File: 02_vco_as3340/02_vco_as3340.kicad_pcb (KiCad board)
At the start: 2 copper layers, 60 x 108 mm, 98 parts, among them J10 SINE OUT, J3 SYNC IN, J4 FM IN, J5 PWM CV IN, J6 1V per O IN, J7 SQUARE OUT, J8 SAW OUT, J9 TRI OUT, Q1 BC847, Q2 BC847, SW2 SW_SPDT, U1 TL072, U2 AS3340, U3 TL074

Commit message: added diodes
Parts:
- added D3: 1N5819WS, Diode_SMD:D_SOD-323, B.Cu at (21.0, 88.3)
- added D4: 1N5819WS, Diode_SMD:D_SOD-323, B.Cu at (37.5, 87.6)
- C7, C8: value 47uF -> 20uF
- SW1: footprint cynthia:switch_linear_1x4 -> cynthia:switch_linear_2x4
- SW2: footprint cynthia:switch -> cynthia:switch_spdt
- moved C7 1.13 mm to (43.2, 88.9), turned to 90 degrees
- moved SW1 0.17 mm to (8.05, 27.2)
- moved C8 0.13 mm to (15.2, 90.7)
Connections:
- H1 pad 1: +12V -> Net-(D4-A)
- H1 pad 10: -12V -> Net-(D3-K)
- H1 pad 2: +12V -> Net-(D4-A)
- H1 pad 9: -12V -> Net-(D3-K)
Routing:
- net Net-(C1-Pad2): track 39.0 -> 29.4 mm
- net Net-(C2-Pad2): track 31.2 -> 23.5 mm
- net Net-(D4-A): track 0.00 -> 6.41 mm
- net Net-(D3-K): track 0.00 -> 5.63 mm
- net -12V: track 157.4 -> 155.4 mm, vias 5 -> 6
- net +12V: track 214.3 -> 213.1 mm, vias 6 -> 7
- net Net-(C3-Pad2): track 12.1 -> 12.6 mm

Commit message: added diodes to 02
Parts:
- C7, C8: value 20uF -> 22uF
- D3, D4: value 1N5819WS -> SS14; footprint Diode_SMD:D_SOD-323 -> Diode_SMD:D_SMA; moved to F.Cu
- moved D3 28.6 mm to (49.5, 87.0)
- moved D4 12.1 mm to (25.5, 89.5)
- moved C7 11.5 mm to (54.0, 85.0), turned to 0 degrees
- moved H1 8.56 mm to (42.5, 87.0)
- moved C8 4.81 mm to (18.8, 87.5), turned to 0 degrees
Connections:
- D3 pad 1: Net-(D3-K) -> +12V
- D3 pad 2: -12V -> Net-(D3-A)
- D4 pad 1: +12V -> Net-(D4-K)
- D4 pad 2: Net-(D4-A) -> -12V
- H1 pad 1: Net-(D4-A) -> Net-(D3-A)
- H1 pad 10: Net-(D3-K) -> Net-(D4-K)
- H1 pad 2: Net-(D4-A) -> Net-(D3-A)
- H1 pad 9: Net-(D3-K) -> Net-(D4-K)
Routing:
- net +12V: track 213.1 -> 193.5 mm, vias 7 -> 8
- net Net-(D3-A): track 0.00 -> 10.5 mm
- net Net-(D4-K): track 0.00 -> 10.2 mm
- net Net-(D4-A): track 6.41 -> 0.00 mm
- net Net-(D3-K): track 5.63 -> 0.00 mm
- net Net-(R40-Pad2): track 68.3 -> 73.5 mm
- net -12V: track 155.4 -> 160.2 mm, vias 6 -> 7
- net Net-(R47-Pad2): track 30.5 -> 32.6 mm
- net Net-(R38-Pad2): track 47.8 -> 47.3 mm

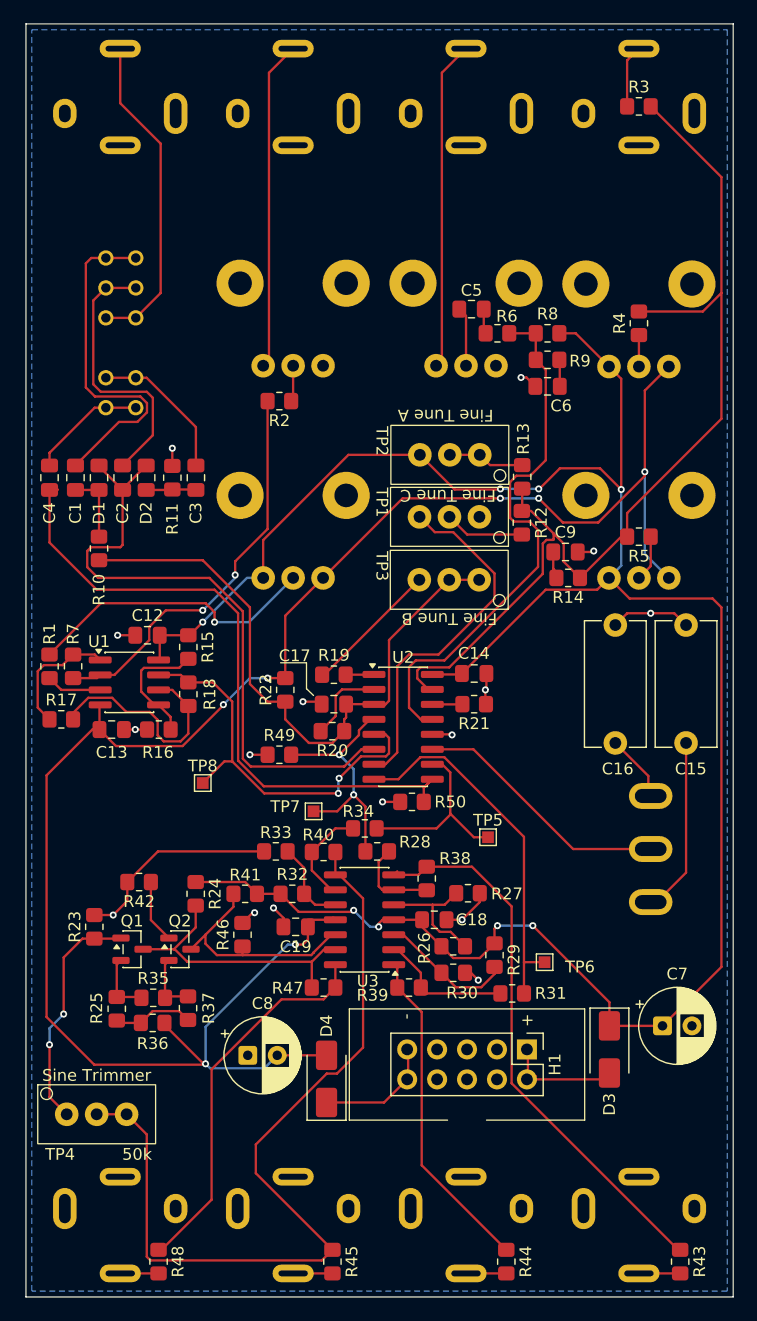
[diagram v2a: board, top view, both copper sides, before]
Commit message: cleaner PCB layout
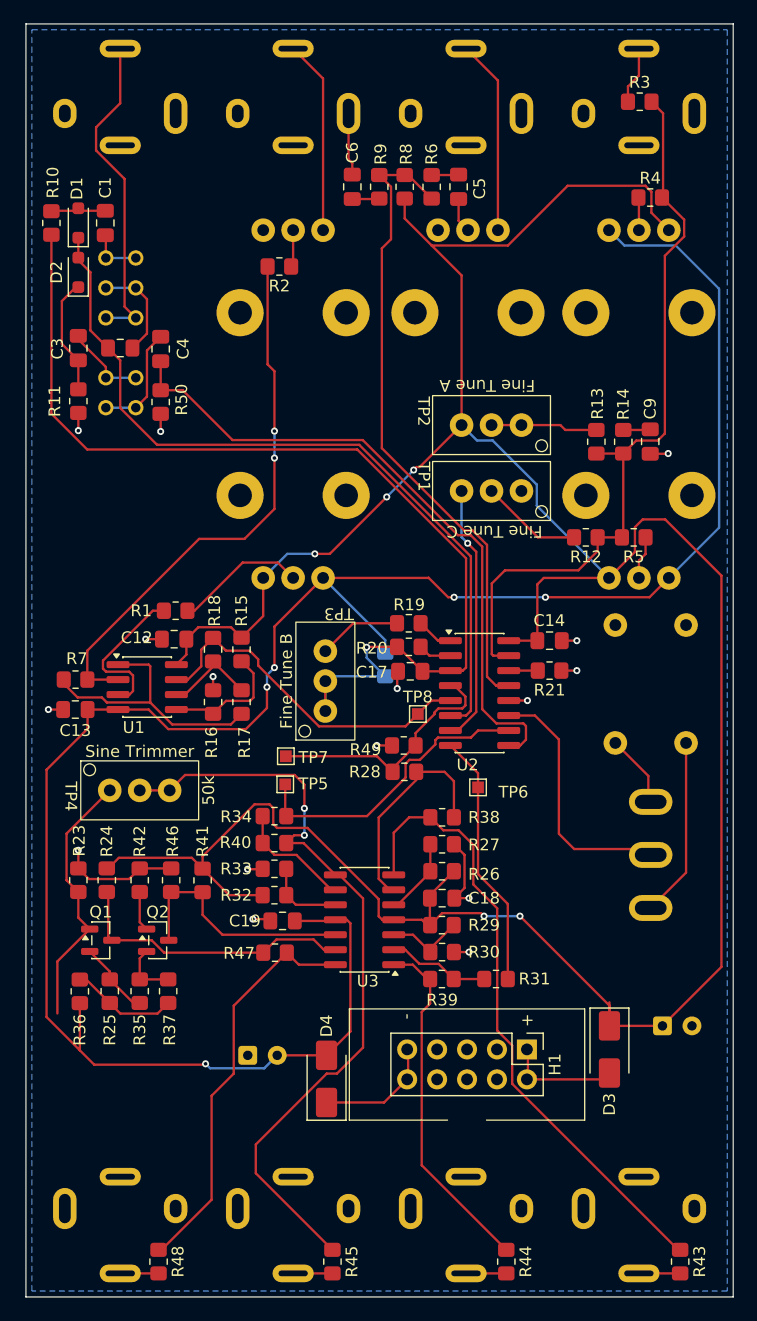
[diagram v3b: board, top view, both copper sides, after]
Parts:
- C15, C16, C7, C8, R22: moved to B.Cu
- D1, D2: footprint cynthia:C SMD 0805 -> Diode_SMD:D_SOD-323_HandSoldering
- moved R50 40.1 mm to (11.4, 32.1), turned to 90 degrees
- moved R10 27.9 mm to (2.16, 16.9)
- moved TP4 27.7 mm to (9.65, 65.0)
- moved C6 23.7 mm to (27.7, 13.8), turned to -90 degrees
- moved C1 21.8 mm to (6.73, 16.9), turned to -90 degrees
- moved D1 21.7 mm to (4.45, 16.9), turned to 90 degrees
- moved R9 20.5 mm to (30.0, 13.8), turned to 90 degrees
- moved TP8 19.2 mm to (33.2, 58.5)
- moved D2 18.3 mm to (4.45, 21.1)
- moved TP5 17.8 mm to (22.0, 64.5)
- moved R8 17.4 mm to (32.1, 13.8), turned to -90 degrees
- moved TP6 15.9 mm to (38.4, 64.8)
- moved R17 15.4 mm to (18.3, 57.5), turned to 90 degrees
- moved C3 14.8 mm to (4.45, 27.5)
- moved C4 14.4 mm to (11.4, 27.6)
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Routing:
- net +12V: track 193.5 -> 245.9 mm, vias 8 -> 5
- net Net-(U2-VEE): track 53.0 -> 87.4 mm, vias 0 -> 1
- net Net-(C1-Pad2): track 29.4 -> 4.49 mm
- net Net-(U2-VFCI): track 86.0 -> 64.6 mm
- net -12V: track 160.2 -> 181.4 mm, vias 7 -> 5
- net Net-(C2-Pad2): track 23.5 -> 8.54 mm
- net Net-(R1-Pad1): track 25.2 -> 11.2 mm, vias 1 -> 0
- net Net-(U1A--): track 34.1 -> 46.7 mm
- net Net-(R17-Pad1): track 10.6 -> 23.1 mm
- net Net-(D1-K): track 54.4 -> 66.7 mm
- net Net-(J5-PadT): track 28.0 -> 16.5 mm
- net Net-(J4-PadT): track 28.0 -> 16.5 mm
- net Net-(U1B--): track 19.3 -> 7.98 mm
- net Net-(U3B--): track 7.54 -> 18.3 mm
- net Net-(U2-VSO): track 31.3 -> 21.8 mm
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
